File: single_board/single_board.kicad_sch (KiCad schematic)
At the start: 81 parts, among them J1 5V, J10 PWM2, J11 PWM3, J12 PWM4, J13 PWM45, J14 PWM6, J15 BOOTSEL, J16 SWD, J17 UART, J18 CAN_OUT, J19 SPI Debug, J2 v3v3, J3 ENC1, J4 ENC2, J5 ENC3, J6 ENC4, J7 ENC5, J8 ENC6, J9 PWM1, SW1 Button, U1 USBLC6-2SC6, U2 AP2112K-3.3, U3 STM32G474VBTx, U4 TJA1042T-3, U5 LSM6DSVTR, Y1 FC-135

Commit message: Updated Power Scheme
+ USBC
+ Fuse
+ Power flags
+ Power symbols, VBUS, 5V, v3v3
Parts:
- removed C14: 22uf, Capacitor_SMD:C_0805_2012Metric, symbol Device:C_Small
- removed C4: 100nF, Capacitor_SMD:C_0402_1005Metric, symbol Device:C_Small
- removed C5: 100nf, Capacitor_SMD:C_0402_1005Metric, symbol Device:C_Small
- removed D5: FM-B2020RGBA-HG, SSS:FM-B2020RGBA-HG, symbol Device:LED_RBAG
- removed J1: 5V, Connector_PinHeader_2.54mm:PinHeader_1x02_P2.54mm_Vertical, symbol Connector_Generic:Conn_01x02
- removed J15: BOOTSEL, Connector_PinHeader_2.54mm:PinHeader_1x02_P2.54mm_Vertical, symbol Connector_Generic:Conn_01x02
- removed J2: v3v3, Connector_PinHeader_2.54mm:PinHeader_1x02_P2.54mm_Vertical, symbol Connector_Generic:Conn_01x02
- removed R10, R9: 470, Resistor_SMD:R_0402_1005Metric, symbol Device:R_Small
- removed U1: USBLC6-2SC6, Package_TO_SOT_SMD:SOT-23-6, symbol Power_Protection:USBLC6-2SC6
- removed U5: LSM6DSVTR, SSS:LSM6DSVTR, symbol SSS:LSM6DSVTR
- added C11: 100nF, Capacitor_SMD:C_0603_1608Metric, symbol Device:C_Small
- added D2: FM-B2020RGBA-HG, symbol Device:LED_RBAG
- added F1: MF-FSMF050X, symbol Device:Polyfuse_Small
- added J2: USB_C_Receptacle_USB2.0_16P, symbol Connector:USB_C_Receptacle_USB2.0_16P
- added J9: BOOTSEL, Connector_PinHeader_2.54mm:PinHeader_1x03_P2.54mm_Vertical, symbol Connector_Generic:Conn_01x03
- added R1, R3, R4, R5: 5.1k, Resistor_SMD:R_0603_1608Metric, symbol Device:R_Small
- added R13: 10k, Resistor_SMD:R_0402_1005Metric, symbol Device:R_Small
- added U3: USBLC6-2SC6, Package_TO_SOT_SMD:SOT-23-6, symbol Power_Protection:USBLC6-2SC6
- added U4: (no value), symbol Rover:LSM6DSV
- R8: value 470 -> 5.1k; footprint Resistor_SMD:R_0402_1005Metric -> Resistor_SMD:R_0603_1608Metric
- Y1: footprint SSS:FC-135seikoEpson -> (none)
- renumbered C23 to C1, C27 to C10, C15 to C12, C16 to C13, C17 to C14, C18 to C15, C20 to C16, C22 to C17, C25 to C18, C28 to C19, C26 to C2, C32 to C20, C33 to C21, C19 to C22, C21 to C23, C9 to C24, C11 to C25, C1 to C26, C2 to C27, C3 to C28, C13 to C29, C7 to C3, C29 to C30, C30 to C31, C6 to C4, C12 to C5, C10 to C6, C8 to C7, C31 to C8, C24 to C9, D4 to D1, D1 to D3, D2 to D4, D3 to D5, J18 to J1, J5 to J10, J17 to J12, J6 to J13, J12 to J14, J7 to J15, J13 to J16, J8 to J17, J14 to J18, J9 to J4, J16 to J5, J4 to J6, J10 to J7, J19 to J8, R1 to R10, R2 to R11, R3 to R12, R4 to R14, R5 to R2, R11 to R6, R6 to R9, U2 to U1, U4 to U2, U3 to U5
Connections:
- net 5V: now also C11.1, D2.3 (A), F1.2, U3.5 (VBUS)
- net BOOT0: now also J9.2 (Pin_2)
- net GND: now also C11.2, J2.A1 (GND), J2.A12 (GND), J2.B1 (GND), J2.B12 (GND), J2.SH (SHIELD), R3.1, R5.1, U3.2 (GND), U4.2 (SDx), U4.3 (SCx), U4.4 (INT1), U4.6 (GND), U4.7 (GND)
- net IMU_MISO: now also U4.1 (SDO/SA0)
- net IMU_MOSI: now also U4.14 (SDA)
- net IMU_NSS: now also U4.12 (CS)
- net IMU_SCK: now also U4.13 (SCL)
- net INT2: now also U4.9 (INT2)
- net TRI_LED_B: now also R8.1
- net TRI_LED_G: now also R4.1
- net TRI_LED_R: now also R1.1; no longer R8.2
- net v3v3: now also R13.1, U4.5 (VDD_IO), U4.8 (VDD)
- net at R14.1: now also J9.1 (Pin_1)
- new net: J2.B5 (CC2), R5.2
- new net: D2.2 (BK), R8.2
- new net: J2.A5 (CC1), R3.2
- new net: J9.3 (Pin_3), R13.2
- new net: D2.1 (RK), R1.2
- new net: J2.A6 (D+), J2.B6 (D+), U3.3 (I/O2)
- new net: J2.A7 (D-), J2.B7 (D-), U3.1 (I/O1)
- new net: D2.4 (GK), R4.2
- new net VBUS: F1.1, J2.A4 (VBUS), J2.A9 (VBUS), J2.B4 (VBUS), J2.B9 (VBUS)
- new net usb-DN: U3.6 (I/O1)
- new net usb-DP: U3.4 (I/O2)
- no-connect marks 7 -> 5
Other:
- note added: "330R not sufficient for 5V. Use 5.1k to reduce number of different components"
- note added: "Choose either termination method 120R Split 60-60R"
- note added: "LDO spec Vout typ 3.3V Iout max 600mA Cin/Cout min 1uF"
- note added: "MCU spec section 5.3.7 R_ext is not needed for OSC32"
- note added: "MODE LED"
- note added: "Mode 0 SPI 4-wire"
- note added: "Perception interface"
- note added: "ST AN2867 - Seiko Epson - 7pf model; Digikey PCB Routing also based on A.N."
- note added: "Text 100mils, 50mils, 30mils"
- note added: "mcu spec 100nf on reset per datasheet see 5.3.15"
- note added: "vbus spec 4.75/5/5.25V @ 500mA"
- note added: "vbus spec max capacitance 10uF"
- note removed: "100nf per datasheet see 5.3.15"
- note removed: "Choose either termination method"
- note removed: "Data line resistors & Current limiting resistors"
- note removed: "INT1 grounded; Difficult to route"
- note removed: "MCU datasheet section 5.3.7 R_ext is not needed for OSC32"
- note removed: "Maybe for perception interface"
- note removed: "Mode 1 SPI 4-wire"
- note removed: "Preserved INT2 For interrupt functionality if needed"
- note removed: "Source: ST AN2867 - Seiko Epson - 7pf model; Digikey PCB Routing also based on A.N."
- moved on the sheet: C12, C13, C14, C15, C16, C17, C18, C19, C20, C21, C22, C23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

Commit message: All elements added
MCU Pinout
GPIO
IMU Pinout
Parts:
- removed C12, C13: 1uf, Capacitor_SMD:C_0402_1005Metric, symbol Device:C_Small
- removed J10: ENC3, Connector_PinHeader_2.54mm:PinHeader_1x04_P2.54mm_Vertical, symbol Connector_Generic:Conn_01x04
- removed J11: PWM3, Connector_PinHeader_2.54mm:PinHeader_1x04_P2.54mm_Vertical, symbol Connector_Generic:Conn_01x04
- removed J13: ENC4, Connector_PinHeader_2.54mm:PinHeader_1x04_P2.54mm_Vertical, symbol Connector_Generic:Conn_01x04
- removed J15: ENC5, Connector_PinHeader_2.54mm:PinHeader_1x04_P2.54mm_Vertical, symbol Connector_Generic:Conn_01x04
- removed J16: PWM45, Connector_PinHeader_2.54mm:PinHeader_1x04_P2.54mm_Vertical, symbol Connector_Generic:Conn_01x04
- removed J18: PWM6, Connector_PinHeader_2.54mm:PinHeader_1x04_P2.54mm_Vertical, symbol Connector_Generic:Conn_01x04
- removed J3: ENC1, Connector_PinHeader_2.54mm:PinHeader_1x04_P2.54mm_Vertical, symbol Connector_Generic:Conn_01x04
- removed J4: PWM1, Connector_PinHeader_2.54mm:PinHeader_1x04_P2.54mm_Vertical, symbol Connector_Generic:Conn_01x04
- removed J5: SWD, Connector_PinHeader_2.54mm:PinHeader_1x04_P2.54mm_Vertical, symbol Connector_Generic:Conn_01x04
- removed J7: PWM2, Connector_PinHeader_2.54mm:PinHeader_1x04_P2.54mm_Vertical, symbol Connector_Generic:Conn_01x04
- added C25, C29, C32: 100nF, Capacitor_SMD:C_0402_1005Metric, symbol Device:C_Small
- added D5, D6: SS14, Diode_SMD:D_SMA, symbol Device:D_Schottky_Small
- added F2: MF-FSMF050X, Fuse:Fuse_0603_1608Metric, symbol Device:Polyfuse_Small
- added J11, J15, J21, J5, J7: Screw_Terminal_01x02, TerminalBlock:TerminalBlock_MaiXu_MX126-5.0-02P_1x02_P5.00mm, symbol Connector:Screw_Terminal_01x02
- added J13, J16, J19, J22, J4, J8: Conn_01x03, Connector_PinHeader_2.54mm:PinHeader_1x03_P2.54mm_Vertical, symbol Connector_Generic:Conn_01x03
- added J20, J23, J9: Conn_01x04, Connector_PinHeader_2.54mm:PinHeader_1x04_P2.54mm_Vertical, symbol Connector_Generic:Conn_01x04
- added J24: Conn_01x05, Connector_PinHeader_2.54mm:PinHeader_1x05_P2.54mm_Vertical, symbol Connector_Generic:Conn_01x05
- added J25: Conn_01x02, Connector_PinHeader_2.54mm:PinHeader_1x02_P2.54mm_Vertical, symbol Connector_Generic:Conn_01x02
- added J26: TC2030, Connector:Tag-Connect_TC2030-IDC-NL_2x03_P1.27mm_Vertical, symbol Connector:TC2030
- added J3: Screw_Terminal_01x03, TerminalBlock:TerminalBlock_MaiXu_MX126-5.0-03P_1x03_P5.00mm, symbol Connector:Screw_Terminal_01x03
- added Q1: 2N7002, Package_TO_SOT_SMD:SOT-23, symbol Transistor_FET:2N7002
- added R12, R24: 10k, Resistor_SMD:R_0402_1005Metric, symbol Device:R_Small
- added R13, R15, R18: 5.1k, Resistor_SMD:R_0603_1608Metric, symbol Device:R_Small
- added R14, R16, R19, R23: 120, Resistor_SMD:R_0402_1005Metric, symbol Device:R_Small
- added R22: 1M, Resistor_SMD:R_0402_1005Metric, symbol Device:R_Small
- C1, C9: value 1uf -> 1uF
- C11: footprint Capacitor_SMD:C_0603_1608Metric -> Capacitor_SMD:C_0402_1005Metric
- C12: renamed from C16; value 100nf -> 100nF
- C13: renamed from C14; value 100nf -> 100nF
- C14: renamed from C15; value 100nf -> 100nF
- C15: renamed from C17; value 100nf -> 100nF
- C16: renamed from C18; value 100nf -> 100nF
- C17: renamed from C19; value 4.7uf -> 4.7uF
- C20: renamed from C22; value 10nf -> 10nF
- C21: renamed from C23; value 1uf -> 1uF
- C22: renamed from C24; value 1uf -> 1uF
- C23: renamed from C25; value 100nf -> 100nF
- C24: renamed from C29; value 100nf -> 100nF
- C26, C27, C28: value 22uf -> 100nF; footprint Capacitor_SMD:C_0805_2012Metric -> Capacitor_SMD:C_0402_1005Metric
- C30, C31: value 8pf -> 8pF
- C4, C5: value 100nf -> 100nF
- C8: value 10nf -> 10nF
- F1: footprint (none) -> Fuse:Fuse_0603_1608Metric
- J10: renamed from J8; now not fitted; now left out of the parts list
- J14: value PWM4 -> Conn_01x04
- J17: value ENC6 -> Conn_01x04
- J2: footprint (none) -> Connector_USB:USB_C_Receptacle_HRO_TYPE-C-31-M-12
- J6: value ENC2 -> Conn_01x04
- U4: value (none) -> LSM6DSV; footprint (none) -> Rover:LSM6DSV
- renumbered C20 to C18, C21 to C19, D5 to D7, J9 to J12, J12 to J18, R3 to R1, R13 to R17, R1 to R2, R12 to R20, R14 to R21, R2 to R3, R5 to R4, R4 to R5
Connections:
- net usb-DN is gone; now on net USB-DN: U3.6 (I/O1)
- net usb-DP is gone; now on net USB-DP: U3.4 (I/O2)
- net 5V: now also J14.4 (Pin_4), J17.4 (Pin_4), J2.A4 (VBUS), J2.A9 (VBUS), J2.B4 (VBUS), J2.B9 (VBUS), J6.4 (Pin_4), C25.1, C29.1, C32.1, D5.1 (K), J20.4 (Pin_4), J23.4 (Pin_4), J9.4 (Pin_4); no longer J14.1 (Pin_1), J17.1 (Pin_1), J6.1 (Pin_1)
- net DIR1: now also U5.18 (PC3), J4.3 (Pin_3); no longer U5.90 (PB3)
- net DIR2: now also U5.26 (PA4), J8.3 (Pin_3); no longer U5.87 (PD5)
- net DIR3: now also U5.5 (PE6), J13.3 (Pin_3); no longer U5.85 (PD3)
- net DIR4: now also U5.68 (PC9), J16.3 (Pin_3); no longer J14.4 (Pin_4), U5.65 (PC6)
- net DIR5: now also U5.61 (PD14), J19.3 (Pin_3); no longer U5.60 (PD13)
- net DIR6: now also U5.97 (PE0), J22.3 (Pin_3); no longer U5.58 (PD11)
- net ENC1_A: now also J6.3 (Pin_3), U5.15 (PC0); no longer U5.2 (PE3)
- net ENC1_B: now also J6.2 (Pin_2), U5.16 (PC1); no longer U5.1 (PE2)
- net ENC2_A: now also U5.20 (PA0), J9.3 (Pin_3); no longer J6.3 (Pin_3), U5.4 (PE5)
- net ENC2_B: now also U5.21 (PA1), J9.2 (Pin_2); no longer J6.4 (Pin_4), U5.3 (PE4)
- net ENC3_A: now also J14.3 (Pin_3), U5.28 (PA6); no longer U5.16 (PC1)
- net ENC3_B: now also J14.2 (Pin_2), U5.29 (PA7); no longer U5.15 (PC0)
- net ENC4_A: now also J17.3 (Pin_3), U5.59 (PD12); no longer U5.17 (PC2)
- net ENC4_B: now also J17.2 (Pin_2), U5.60 (PD13); no longer U5.18 (PC3)
- net ENC5_A: now also U5.65 (PC6), J20.3 (Pin_3); no longer U5.20 (PA0)
- net ENC5_B: now also U5.66 (PC7), J20.2 (Pin_2); no longer U5.21 (PA1)
- net ENC6_A: now also U5.1 (PE2), J23.3 (Pin_3); no longer J17.3 (Pin_3), U5.22 (PA2)
- net ENC6_B: now also U5.2 (PE3), J23.2 (Pin_2); no longer J17.4 (Pin_4), U5.25 (PA3)
- net GND: now also J14.1 (Pin_1), J17.1 (Pin_1), J6.1 (Pin_1), C25.2, C29.2, C32.2, D5.2 (A), D6.2 (A), J11.1 (Pin_1), J13.1 (Pin_1), J16.1 (Pin_1), J19.1 (Pin_1), J20.1 (Pin_1), J22.1 (Pin_1), J23.1 (Pin_1), J24.2 (Pin_2), J25.1 (Pin_1), J26.6, J3.1 (Pin_1), J4.1 (Pin_1), J5.1 (Pin_1), J7.1 (Pin_1), J8.1 (Pin_1), J9.1 (Pin_1), R12.2, R22.2, R24.2; no longer J14.2 (Pin_2), J17.2 (Pin_2), J6.2 (Pin_2), SW1.1, U4.4 (INT1)
- net HEARTBEAT: now also U5.42 (PE11); no longer U5.71 (PA10)
- net IMU_MISO: now also U5.91 (PB4); no longer U5.28 (PA6)
- net IMU_MOSI: now also U5.81 (PC12); no longer U5.29 (PA7)
- net IMU_NSS: now also U5.89 (PD7); no longer U5.26 (PA4)
- net IMU_SCK: now also U5.90 (PB3); no longer U5.27 (PA5)
- net INT2: now also U5.86 (PD4); no longer U5.30 (PC4)
- net PWM1: now also U5.17 (PC2), J4.2 (Pin_2); no longer U5.89 (PD7)
- net PWM2: now also U5.25 (PA3), J8.2 (Pin_2); no longer U5.88 (PD6)
- net PWM3: now also U5.4 (PE5), J13.2 (Pin_2); no longer U5.86 (PD4)
- net PWM4: now also U5.67 (PC8), J16.2 (Pin_2); no longer J14.3 (Pin_3), U5.62 (PD15)
- net PWM5: now also U5.62 (PD15), J19.2 (Pin_2); no longer U5.61 (PD14)
- net PWM6: now also U5.98 (PE1), J22.2 (Pin_2); no longer U5.59 (PD12)
- net RST: now also J24.3 (Pin_3), J26.1
- net SWCLK: now also J24.5 (Pin_5), J26.5
- net SWDIO: now also J24.4 (Pin_4), J26.3
- net TRI_LED_B: now also U5.93 (PB6); no longer U5.70 (PA9)
- net TRI_LED_G: now also U5.94 (PB7); no longer U5.68 (PC9)
- net TRI_LED_R: now also U5.92 (PB5); no longer U5.69 (PA8)
- net v3v3: now also D6.1 (K), F2.2, J15.2 (Pin_2), J21.2 (Pin_2), J24.1 (Pin_1), J26.2, R13.1, R15.1, R18.1
- net LS1: now reaches U5.39 (PE8)
- net LS1: now also R14.2
- net LS2: now reaches U5.40 (PE9)
- net LS2: now also R16.2
- net LS3: now reaches U5.41 (PE10)
- net LS3: now also R19.2
- net FSR: now reaches U5.45 (PE14)
- net FSR: now also J15.1 (Pin_1), R22.1
- net LASER_SIG: now reaches U5.46 (PE15)
- net LASER_SIG: now also R23.1
- net USB-DN: now reaches U5.72 (PA11)
- net USB-DP: now reaches U5.73 (PA12)
- removed net VBUS: F1.1, J2.A4 (VBUS), J2.A9 (VBUS), J2.B4 (VBUS), J2.B9 (VBUS)
- new net: Q1.2 (S), R24.1
- new net: Q1.1 (G), R23.2
- new net: J21.1 (Pin_1), Q1.3 (D)
- new net: R12.1, SW1.1
- new net 5VIN: F1.1, J25.2 (Pin_2), J3.3 (Pin_3)
- new net INT1: U4.4 (INT1), U5.85 (PD3)
- new net LimitSwitch1: J5.2 (Pin_2), R13.2, R14.1
- new net LimitSwitch2: J7.2 (Pin_2), R15.2, R16.1
- new net LimitSwitch3: J11.2 (Pin_2), R18.2, R19.1
- new net v3v3IN: F2.1, J3.2 (Pin_2)
- no-connect marks 5 -> 6
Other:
- note added: "Absolute for DC motors, 1 encoder per motor May use quadrature instead of absolute for some stepper motors"
- note added: "Analog, ADC4 1IN"
- note added: "Different IDC"
- note added: "ESD protection"
- note added: "Encoders"
- note added: "Laser Diode 2.8-5.2V 25mA max draw"
- note added: "Power Supply In"
- note added: "SSS Rover Single Control Board"
- note added: "TIM1 CH1,2 PWM read"
- note added: "TIM1 CH3, PWM generate"
- note added: "TIM2 CH1,2 PWM read"
- note added: "TIM2 CH4, PWM generate"
- note added: "TIM20 CH1,2 PWM read"
- note added: "TIM20 CH4, PWM generate"
- note added: "TIM3 CH1,2 PWM read"
- note added: "TIM3 CH4, PWM generate"
- note added: "TIM4 CH1,2 PWM read"
- note added: "TIM4 CH4, PWM generate"
- note added: "TIM8 CH1,2 PWM read"
- note added: "TIM8 CH3, PWM generate"
- note added: "USBC for programming and standalone testing"
- note added: "Use only PWM read channel for absolute; Pin type from Encoder Mode to PWM Input on CHx."
- note added: "Voltage divider unloaded resistance is stated to be >20M"
- note added: "pretty big diodes protection circuit likely overkill"
- note removed: "Bulk capaciter per header group"
- note removed: "Extra 1uf decoupling"
- note removed: "No power on header; easier routing"
- note removed: "POWER LED"
- note removed: "PWM Control"
- note removed: "PWM and DIR change header pinout for easier routing"
- moved on the sheet: C1, C10, C11, C12, C13, C14, C15, C16, C17, C18, C19, C2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

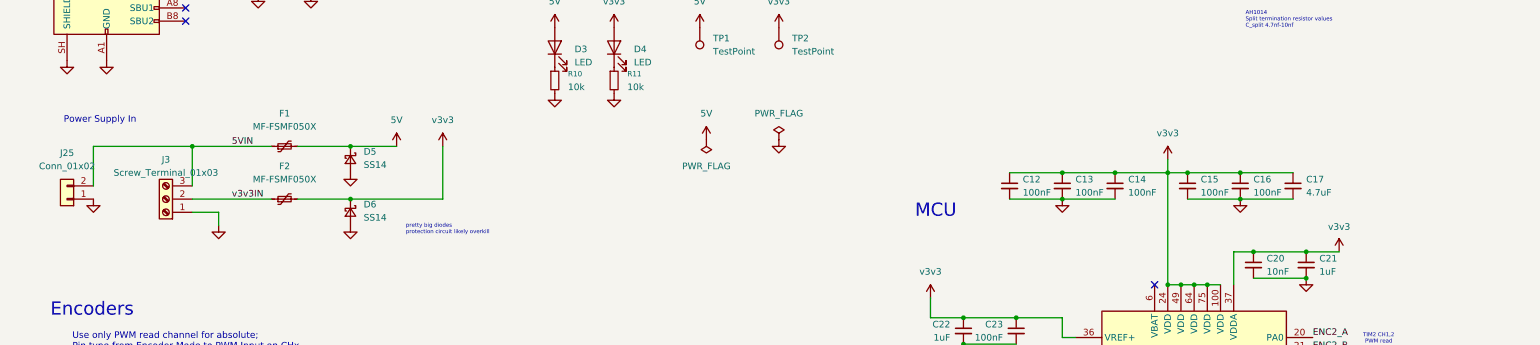
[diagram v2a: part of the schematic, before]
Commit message: Change MCU Power
4.7uf into individual 1uf
Change reverse polarity protection diodes
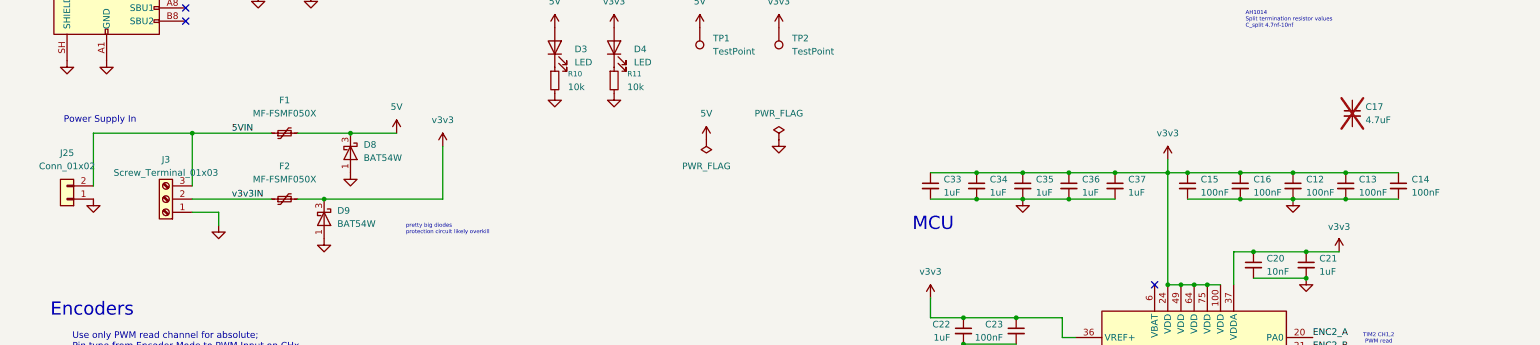
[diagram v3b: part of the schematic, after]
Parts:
- removed D5, D6: SS14, Diode_SMD:D_SMA, symbol Device:D_Schottky_Small
- added C33, C34, C35, C36, C37: 1uF, Capacitor_SMD:C_0402_1005Metric, symbol Device:C_Small
- added D8, D9: BAT54W, Package_TO_SOT_SMD:SOT-323_SC-70, symbol Diode:BAT54W
- C17: now not fitted; now left out of the parts list
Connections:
- net 5V: now also D8.3 (K)
- net GND: now also C33.2, C34.2, C35.2, C36.2, C37.2, D8.1 (A), D9.1 (A); no longer C17.2
- net v3v3: now also C33.1, C34.1, C35.1, C36.1, C37.1, D9.3 (K); no longer C17.1
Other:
- moved on the sheet: C12, C13, C14, F1

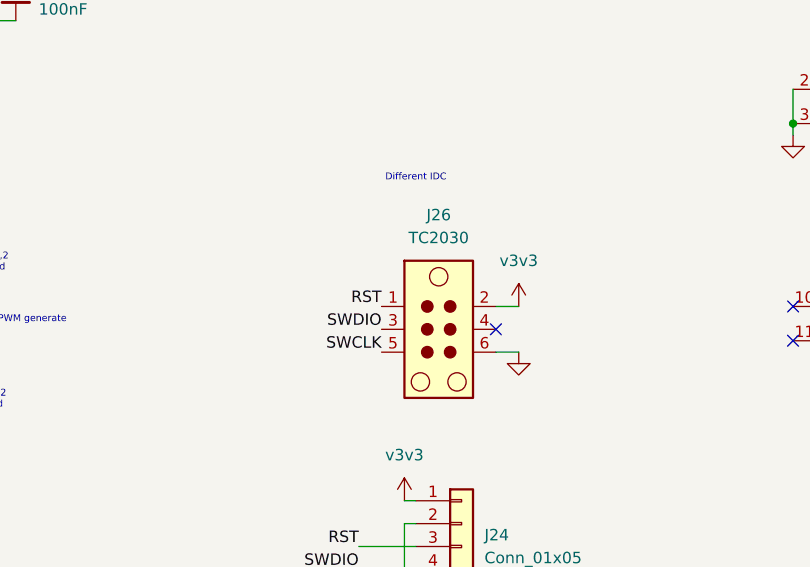
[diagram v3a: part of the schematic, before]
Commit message: Added new footprints
Tri color led
Crystal
Debug
IMU
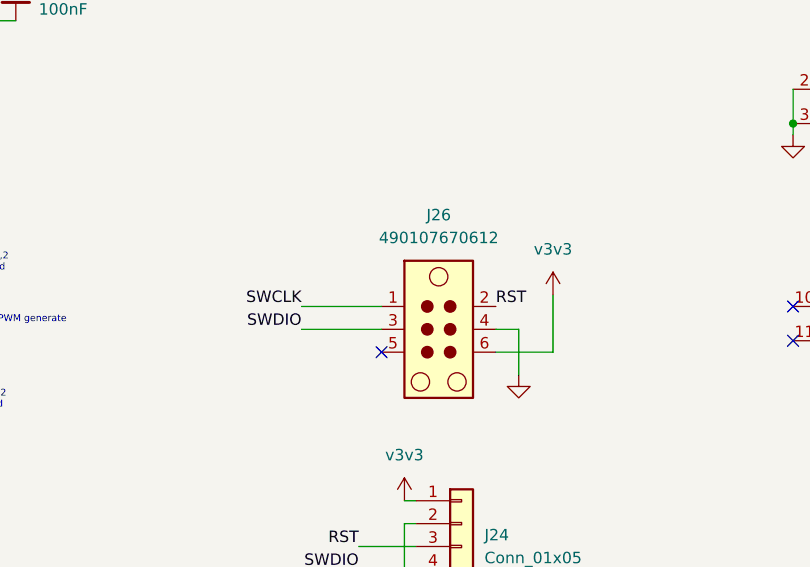
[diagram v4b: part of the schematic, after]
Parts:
- C1, C10, C11, C12, C13, C14, C15, C16, C18, C19, C2, C20, C21, C22, C23, C24, C25, C26, C27, C28, C29, C3, C30, C31, C32, C33, C34, C35, C36, C37, C4, C5, C6, C7, C8, C9: footprint Capacitor_SMD:C_0402_1005Metric -> Capacitor_SMD:C_0402_1005Metric_Pad0.74x0.62mm_HandSolder
- D1, D3, D4, D7: footprint LED_SMD:LED_0603_1608Metric -> LED_SMD:LED_0603_1608Metric_Pad1.05x0.95mm_HandSolder
- D2: footprint (none) -> Rover:FM-B2020RGBA-HG Hand Solder
- F1, F2: footprint Fuse:Fuse_0603_1608Metric -> Fuse:Fuse_0603_1608Metric_Pad1.05x0.95mm_HandSolder
- J26: value TC2030 -> 490107670612; footprint Connector:Tag-Connect_TC2030-IDC-NL_2x03_P1.27mm_Vertical -> Rover:490107670612
- R1, R13, R15, R18, R2, R4, R5, R8: footprint Resistor_SMD:R_0603_1608Metric -> Resistor_SMD:R_0603_1608Metric_Pad0.98x0.95mm_HandSolder
- R10, R11, R12, R14, R16, R17, R19, R20, R21, R22, R23, R24, R3, R6, R7, R9: footprint Resistor_SMD:R_0402_1005Metric -> Resistor_SMD:R_0402_1005Metric_Pad0.72x0.64mm_HandSolder
- Y1: footprint (none) -> Rover:FC-135 Hand Solder
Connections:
- net GND: now also J26.4; no longer J26.6
- net RST: now also J26.2; no longer J26.1
- net SWCLK: now also J26.1; no longer J26.5
- net v3v3: now also J26.6; no longer J26.2
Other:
- note removed: "Different IDC"
